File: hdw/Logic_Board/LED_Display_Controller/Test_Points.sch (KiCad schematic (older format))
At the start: 12 parts, among them J3001 USB UART, J3002 WIFI UART, J3003 FLASH SPI, J3004 Panel TP

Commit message: Finished first pass of digikey part numbers
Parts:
- added TP3009, TP3010: TP, symbol Custom_Library:TP
- J3004: Digi-Key PN (none) -> S2011EC-17-ND
- TP3007: value TestPoint -> TP
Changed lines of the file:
@@
 AR Path="/5BBF5233/5BBFA781" Ref="TP3007"  Part="1"
 F 0 "TP3007" H 4680 6260 50  0000 C CNN
-F 1 "TestPoint" H 4680 6250 50  0001 C CNN
+F 1 "TP" H 4680 6250 50  0001 C CNN
 F 2 "" H 4880 6050 50  0001 C CNN
 F 3 "~" H 4880 6050 50  0001 C CNN
@@
 F 2 "" H 8670 3350 50  0001 C CNN
 F 3 "~" H 8670 3350 50  0001 C CNN
+F 4 "S2011EC-17-ND" H 0   0   50  0001 C CNN "Digi-Key PN"
 	1    8670 3350
 	1    0    0    -1
@@
 	1    0    0    -1
 $EndComp
+$Comp
+L Custom_Library:TP TP?
+U 1 1 5C0ACA52
+P 1260 5980
+AR Path="/5BAAE0FA/5C0ACA52" Ref="TP?"  Part="1"
+AR Path="/5BBF5233/5C0ACA52" Ref="TP3010"  Part="1"
+F 0 "TP3010" H 1260 6130 50  0000 C CNN
+F 1 "TP" H 1260 6130 50  0001 C CNN
+F 2 "" H 1260 5980 60  0000 C CNN
+F 3 "" H 1260 5980 60  0000 C CNN
+	1    1260 5980
+	1    0    0    -1
+$EndComp
+$Comp
+L power:GND #PWR?
+U 1 1 5C0ACA59
+P 1260 5980
+AR Path="/5BAAE0FA/5C0ACA59" Ref="#PWR?"  Part="1"
+AR Path="/5BBF5233/5C0ACA59" Ref="#PWR03015"  Part="1"
+F 0 "#PWR03015" H 1260 5730 50  0001 C CNN
+F 1 "GND" H 1260 5830 50  0000 C CNN
+F 2 "" H 1260 5980 50  0001 C CNN
+F 3 "" H 1260 5980 50  0001 C CNN
+	1    1260 5980
+	1    0    0    -1
+$EndComp
+$Comp
+L Custom_Library:TP TP?
+U 1 1 5C0ACABF
+P 900 5980
+AR Path="/5BAAE0FA/5C0ACABF" Ref="TP?"  Part="1"
+AR Path="/5BBF5233/5C0ACABF" Ref="TP3009"  Part="1"
+F 0 "TP3009" H 900 6130 50  0000 C CNN
+F 1 "TP" H 900 6130 50  0001 C CNN
+F 2 "" H 900 5980 60  0000 C CNN
+F 3 "" H 900 5980 60  0000 C CNN
+	1    900  5980
+	1    0    0    -1
+$EndComp
+$Comp
+L power:GND #PWR?
+U 1 1 5C0ACAC6
+P 900 5980
+AR Path="/5BAAE0FA/5C0ACAC6" Ref="#PWR?"  Part="1"
+AR Path="/5BBF5233/5C0ACAC6" Ref="#PWR03014"  Part="1"
+F 0 "#PWR03014" H 900 5730 50  0001 C CNN
+F 1 "GND" H 900 5830 50  0000 C CNN
+F 2 "" H 900 5980 50  0001 C CNN
+F 3 "" H 900 5980 50  0001 C CNN
+	1    900  5980
+	1    0    0    -1
+$EndComp

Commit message: First pass assignment of footprints to all components
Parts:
- J3001, J3002: footprint (none) -> Pin_Headers:Pin_Header_Straight_1x03_Pitch2.54mm
- J3003: footprint (none) -> Pin_Headers:Pin_Header_Straight_1x04_Pitch2.54mm
- J3004: footprint (none) -> Pin_Headers:Pin_Header_Straight_2x17_Pitch2.54mm
- TP3001, TP3007, TP3009, TP3010: footprint (none) -> Pin_Headers:Pin_Header_Angled_1x01_Pitch2.54mm
- TP3002, TP3003, TP3004, TP3005, TP3006, TP3008: footprint (none) -> Measurement_Points:Measurement_Point_Round-SMD-Pad_Small
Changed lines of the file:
@@
 F 0 "J3001" H 2060 2042 50  0000 L CNN
 F 1 "USB UART" H 2060 1951 50  0000 L CNN
-F 2 "" H 1980 2000 50  0001 C CNN
+F 2 "Pin_Headers:Pin_Header_Straight_1x03_Pitch2.54mm" H 1980 2000 50  0001 C CNN
 F 3 "~" H 1980 2000 50  0001 C CNN
 	1    1980 2000
@@
 F 0 "TP3001" H 1640 6130 50  0000 C CNN
 F 1 "TP" H 1640 6130 50  0001 C CNN
-F 2 "" H 1640 5980 60  0000 C CNN
+F 2 "Pin_Headers:Pin_Header_Angled_1x01_Pitch2.54mm" H 1640 5980 60  0001 C CNN
 F 3 "" H 1640 5980 60  0000 C CNN
 	1    1640 5980
@@
 F 0 "TP3002" H 2040 6130 50  0000 C CNN
 F 1 "TP" H 2040 6130 50  0001 C CNN
-F 2 "" H 2040 5980 60  0000 C CNN
+F 2 "Measurement_Points:Measurement_Point_Round-SMD-Pad_Small" H 2040 5980 60  0001 C CNN
 F 3 "" H 2040 5980 60  0000 C CNN
 	1    2040 5980
@@
 F 0 "TP3003" H 2480 6130 50  0000 C CNN
 F 1 "TP" H 2480 6130 50  0001 C CNN
-F 2 "" H 2480 5980 60  0000 C CNN
+F 2 "Measurement_Points:Measurement_Point_Round-SMD-Pad_Small" H 2480 5980 60  0001 C CNN
 F 3 "" H 2480 5980 60  0000 C CNN
 	1    2480 5980
@@
 F 0 "TP3007" H 4680 6260 50  0000 C CNN
 F 1 "TP" H 4680 6250 50  0001 C CNN
-F 2 "" H 4880 6050 50  0001 C CNN
+F 2 "Pin_Headers:Pin_Header_Angled_1x01_Pitch2.54mm" H 4880 6050 50  0001 C CNN
 F 3 "~" H 4880 6050 50  0001 C CNN
 	1    4680 6050
@@
 F 0 "TP3008" H 5330 6160 50  0000 C CNN
 F 1 "TP" H 5330 6160 50  0001 C CNN
-F 2 "" H 5330 6010 60  0000 C CNN
+F 2 "Measurement_Points:Measurement_Point_Round-SMD-Pad_Small" H 5330 6010 60  0001 C CNN
 F 3 "" H 5330 6010 60  0000 C CNN
 	1    5330 6010
@@
 F 0 "J3004" H 8720 4250 50  0000 C CNN
 F 1 "Panel TP" H 8720 2450 50  0000 C CNN
-F 2 "" H 8670 3350 50  0001 C CNN
+F 2 "Pin_Headers:Pin_Header_Straight_2x17_Pitch2.54mm" H 8670 3350 50  0001 C CNN
 F 3 "~" H 8670 3350 50  0001 C CNN
 F 4 "S2011EC-17-ND" H 0   0   50  0001 C CNN "Digi-Key PN"
@@
 F 0 "TP3004" H 2940 6130 50  0000 C CNN
 F 1 "TP" H 2940 6130 50  0001 C CNN
-F 2 "" H 2940 5980 60  0000 C CNN
+F 2 "Measurement_Points:Measurement_Point_Round-SMD-Pad_Small" H 2940 5980 60  0001 C CNN
 F 3 "" H 2940 5980 60  0000 C CNN
 	1    2940 5980
@@
 F 0 "J3002" H 3700 2042 50  0000 L CNN
 F 1 "WIFI UART" H 3700 1951 50  0000 L CNN
-F 2 "" H 3620 2000 50  0001 C CNN
+F 2 "Pin_Headers:Pin_Header_Straight_1x03_Pitch2.54mm" H 3620 2000 50  0001 C CNN
 F 3 "~" H 3620 2000 50  0001 C CNN
 	1    3620 2000
@@
 F 0 "J3003" H 5260 1992 50  0000 L CNN
 F 1 "FLASH SPI" H 5260 1901 50  0000 L CNN
-F 2 "" H 5180 2000 50  0001 C CNN
+F 2 "Pin_Headers:Pin_Header_Straight_1x04_Pitch2.54mm" H 5180 2000 50  0001 C CNN
 F 3 "~" H 5180 2000 50  0001 C CNN
 	1    5180 2000
@@
 F 0 "TP3005" H 3340 6130 50  0000 C CNN
 F 1 "TP" H 3340 6130 50  0001 C CNN
-F 2 "" H 3340 5980 60  0000 C CNN
+F 2 "Measurement_Points:Measurement_Point_Round-SMD-Pad_Small" H 3340 5980 60  0001 C CNN
 F 3 "" H 3340 5980 60  0000 C CNN
 	1    3340 5980
@@
 F 0 "TP3006" H 3680 6130 50  0000 C CNN
 F 1 "TP" H 3680 6130 50  0001 C CNN
-F 2 "" H 3680 5980 60  0000 C CNN
+F 2 "Measurement_Points:Measurement_Point_Round-SMD-Pad_Small" H 3680 5980 60  0001 C CNN
 F 3 "" H 3680 5980 60  0000 C CNN
 	1    3680 5980
@@
 F 0 "TP3010" H 1260 6130 50  0000 C CNN
 F 1 "TP" H 1260 6130 50  0001 C CNN
-F 2 "" H 1260 5980 60  0000 C CNN
+F 2 "Pin_Headers:Pin_Header_Angled_1x01_Pitch2.54mm" H 1260 5980 60  0001 C CNN
 F 3 "" H 1260 5980 60  0000 C CNN
 	1    1260 5980
@@
 F 0 "TP3009" H 900 6130 50  0000 C CNN
 F 1 "TP" H 900 6130 50  0001 C CNN
-F 2 "" H 900 5980 60  0000 C CNN
+F 2 "Pin_Headers:Pin_Header_Angled_1x01_Pitch2.54mm" H 900 5980 60  0001 C CNN
 F 3 "" H 900 5980 60  0000 C CNN
 	1    900  5980

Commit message: Resolved a few library dependencies
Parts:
- TP3001, TP3002, TP3003, TP3004, TP3005, TP3006, TP3008, TP3009, TP3010: symbol Custom_Library:TP -> LED_Display_Local_Library:TP
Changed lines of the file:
@@
 $EndComp
 $Comp
-L Custom_Library:TP TP?
+L LED_Display_Local_Library:TP TP?
 U 1 1 5BBF8ECA
 P 1640 5980
@@
 $EndComp
 $Comp
-L Custom_Library:TP TP?
+L LED_Display_Local_Library:TP TP?
 U 1 1 5BBF9883
 P 2040 5980
@@
 $EndComp
 $Comp
-L Custom_Library:TP TP?
+L LED_Display_Local_Library:TP TP?
 U 1 1 5BBF98E5
 P 2480 5980
@@
 $EndComp
 $Comp
-L Custom_Library:TP TP3008
+L LED_Display_Local_Library:TP TP3008
 U 1 1 5BBFB09C
 P 5330 6010
@@
 $EndComp
 $Comp
-L Custom_Library:+5V_USB #PWR03011
+L LED_Display_Local_Library:+5V_USB #PWR03011
 U 1 1 5BBFB102
 P 5330 6010
@@
 	9050 4150 8970 4150
 $Comp
-L Custom_Library:TP TP?
+L LED_Display_Local_Library:TP TP?
 U 1 1 5BD1E3B2
 P 2940 5980
@@
 FLASH_MISO
 $Comp
-L Custom_Library:TP TP?
+L LED_Display_Local_Library:TP TP?
 U 1 1 5BF9B560
 P 3340 5980
@@
 $EndComp
 $Comp
-L Custom_Library:TP TP?
+L LED_Display_Local_Library:TP TP?
 U 1 1 5BF9B60D
 P 3680 5980
@@
 $EndComp
 $Comp
-L Custom_Library:+5.5V #PWR03008
+L LED_Display_Local_Library:+5.5V #PWR03008
 U 1 1 5BF9B68F
 P 3680 5980
@@
 $EndComp
 $Comp
-L Custom_Library:TP TP?
+L LED_Display_Local_Library:TP TP?
 U 1 1 5C0ACA52
 P 1260 5980
@@
 $EndComp
 $Comp
-L Custom_Library:TP TP?
+L LED_Display_Local_Library:TP TP?
 U 1 1 5C0ACABF
 P 900 5980

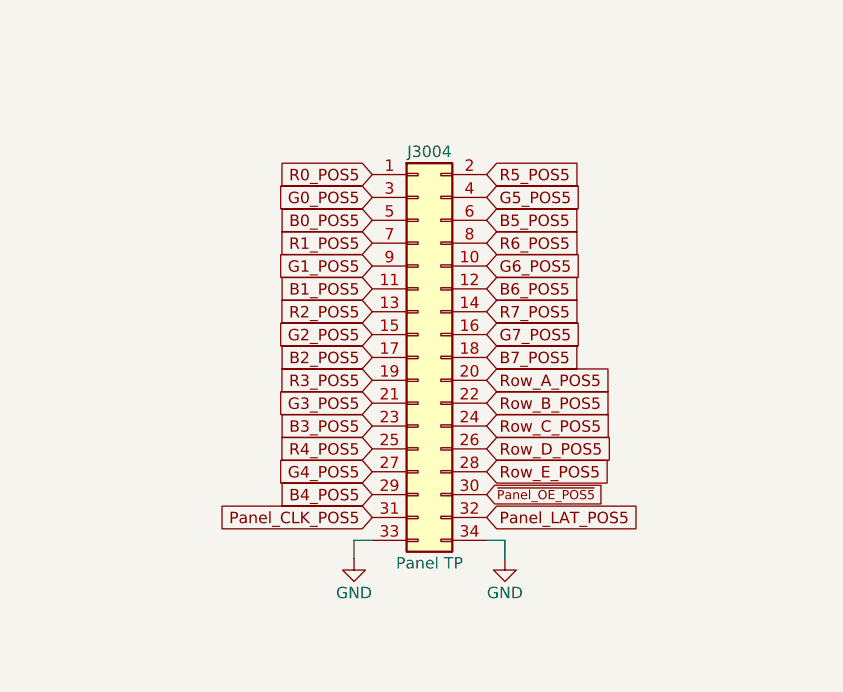
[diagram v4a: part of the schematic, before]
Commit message: Placed more parts, added some labels
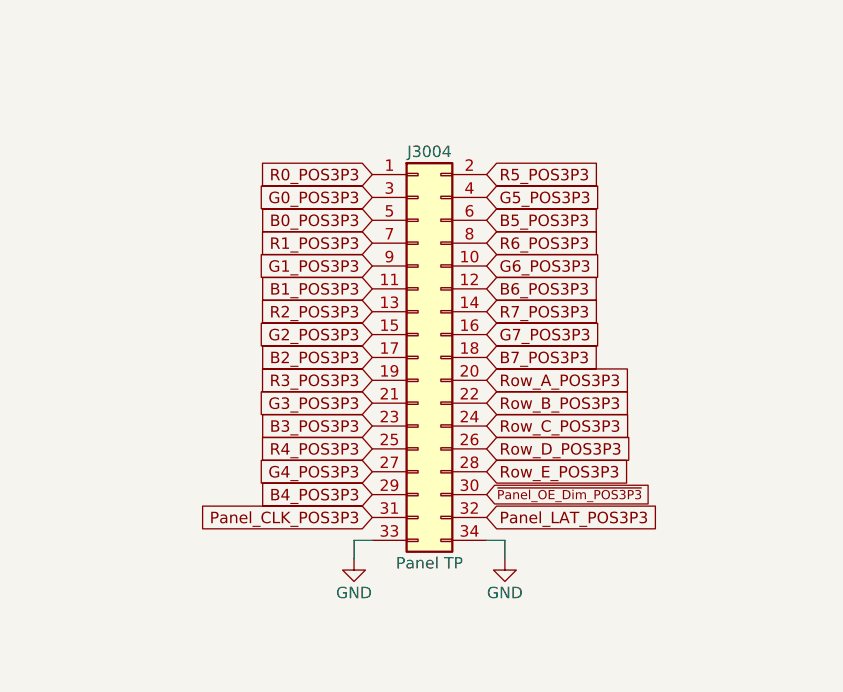
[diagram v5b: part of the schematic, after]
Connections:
- net B0_POS5 renamed B0_POS3P3
- net B1_POS5 renamed B1_POS3P3
- net B2_POS5 renamed B2_POS3P3
- net B3_POS5 renamed B3_POS3P3
- net B4_POS5 renamed B4_POS3P3
- net B5_POS5 renamed B5_POS3P3
- net B6_POS5 renamed B6_POS3P3
- net B7_POS5 renamed B7_POS3P3
- net G0_POS5 renamed G0_POS3P3
- net G1_POS5 renamed G1_POS3P3
- net G2_POS5 renamed G2_POS3P3
- net G3_POS5 renamed G3_POS3P3
- net G4_POS5 renamed G4_POS3P3
- net G5_POS5 renamed G5_POS3P3
- net G6_POS5 renamed G6_POS3P3
- net G7_POS5 renamed G7_POS3P3
- net Panel_CLK_POS5 renamed Panel_CLK_POS3P3
- net Panel_LAT_POS5 renamed Panel_LAT_POS3P3
- net R0_POS5 renamed R0_POS3P3
- net R1_POS5 renamed R1_POS3P3
- net R2_POS5 renamed R2_POS3P3
- net R3_POS5 renamed R3_POS3P3
- net R4_POS5 renamed R4_POS3P3
- net R5_POS5 renamed R5_POS3P3
- net R6_POS5 renamed R6_POS3P3
- net R7_POS5 renamed R7_POS3P3
- net Row_A_POS5 renamed Row_A_POS3P3
- net Row_B_POS5 renamed Row_B_POS3P3
- net Row_C_POS5 renamed Row_C_POS3P3
- net Row_D_POS5 renamed Row_D_POS3P3
- net Row_E_POS5 renamed Row_E_POS3P3
- net ~Panel_OE_POS5 renamed ~Panel_OE_Dim_POS3P3
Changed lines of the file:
@@
 $EndComp
 Text GLabel 8970 3250 2    50   Input ~ 0
-G7_POS5
+G7_POS3P3
 Text GLabel 8970 3350 2    50   Input ~ 0
-B7_POS5
+B7_POS3P3
 Text GLabel 8970 3150 2    50   Input ~ 0
-R7_POS5
+R7_POS3P3
 Text GLabel 8970 2950 2    50   Input ~ 0
-G6_POS5
+G6_POS3P3
 Text GLabel 8970 3050 2    50   Input ~ 0
-B6_POS5
+B6_POS3P3
 Text GLabel 8970 2850 2    50   Input ~ 0
-R6_POS5
+R6_POS3P3
 Text GLabel 8970 2650 2    50   Input ~ 0
-G5_POS5
+G5_POS3P3
 Text GLabel 8970 2750 2    50   Input ~ 0
-B5_POS5
+B5_POS3P3
 Text GLabel 8970 2550 2    50   Input ~ 0
-R5_POS5
+R5_POS3P3
 Text GLabel 8470 3850 0    50   Input ~ 0
-G4_POS5
+G4_POS3P3
 Text GLabel 8470 3950 0    50   Input ~ 0
-B4_POS5
+B4_POS3P3
 Text GLabel 8470 3750 0    50   Input ~ 0
-R4_POS5
+R4_POS3P3
 Text GLabel 8470 3550 0    50   Input ~ 0
-G3_POS5
+G3_POS3P3
 Text GLabel 8470 3650 0    50   Input ~ 0
-B3_POS5
+B3_POS3P3
 Text GLabel 8470 3450 0    50   Input ~ 0
-R3_POS5
+R3_POS3P3
 Text GLabel 8470 3250 0    50   Input ~ 0
-G2_POS5
+G2_POS3P3
 Text GLabel 8470 3350 0    50   Input ~ 0
-B2_POS5
+B2_POS3P3
 Text GLabel 8470 3150 0    50   Input ~ 0
-R2_POS5
+R2_POS3P3
 Text GLabel 8470 2950 0    50   Input ~ 0
-G1_POS5
+G1_POS3P3
 Text GLabel 8470 2650 0    50   Input ~ 0
-G0_POS5
+G0_POS3P3
 Text GLabel 8470 3050 0    50   Input ~ 0
-B1_POS5
+B1_POS3P3
 Text GLabel 8470 2850 0    50   Input ~ 0
-R1_POS5
+R1_POS3P3
 Text GLabel 8470 2750 0    50   Input ~ 0
-B0_POS5
+B0_POS3P3
 Text GLabel 8470 2550 0    50   Input ~ 0
-R0_POS5
+R0_POS3P3
 Text GLabel 8970 4050 2    50   Input ~ 0
-Panel_LAT_POS5
+Panel_LAT_POS3P3
+Text GLabel 8470 4050 0    50   Input ~ 0
+Panel_CLK_POS3P3
+Text GLabel 8970 3650 2    50   Input ~ 0
+Row_C_POS3P3
+Text GLabel 8970 3850 2    50   Input ~ 0
+Row_E_POS3P3
+Text GLabel 8970 3750 2    50   Input ~ 0
+Row_D_POS3P3
+Text GLabel 8970 3550 2    50   Input ~ 0
+Row_B_POS3P3
+Text GLabel 8970 3450 2    50   Input ~ 0
+Row_A_POS3P3
 Text GLabel 8970 3950 2    40   Input ~ 0
-~Panel_OE_POS5
-Text GLabel 8470 4050 0    50   Input ~ 0
-Panel_CLK_POS5
-Text GLabel 8970 3650 2    50   Input ~ 0
-Row_C_POS5
-Text GLabel 8970 3850 2    50   Input ~ 0
-Row_E_POS5
-Text GLabel 8970 3750 2    50   Input ~ 0
-Row_D_POS5
-Text GLabel 8970 3550 2    50   Input ~ 0
-Row_B_POS5
-Text GLabel 8970 3450 2    50   Input ~ 0
-Row_A_POS5
+~Panel_OE_Dim_POS3P3
 $EndSCHEMATC

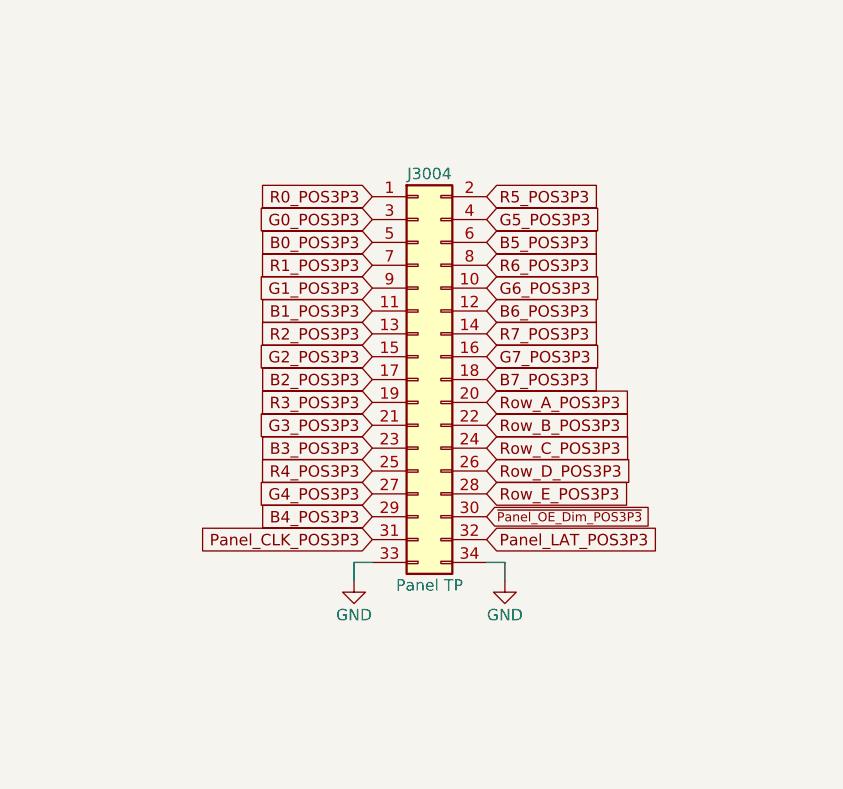
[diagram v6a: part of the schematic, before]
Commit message: Routed a bunch of traces
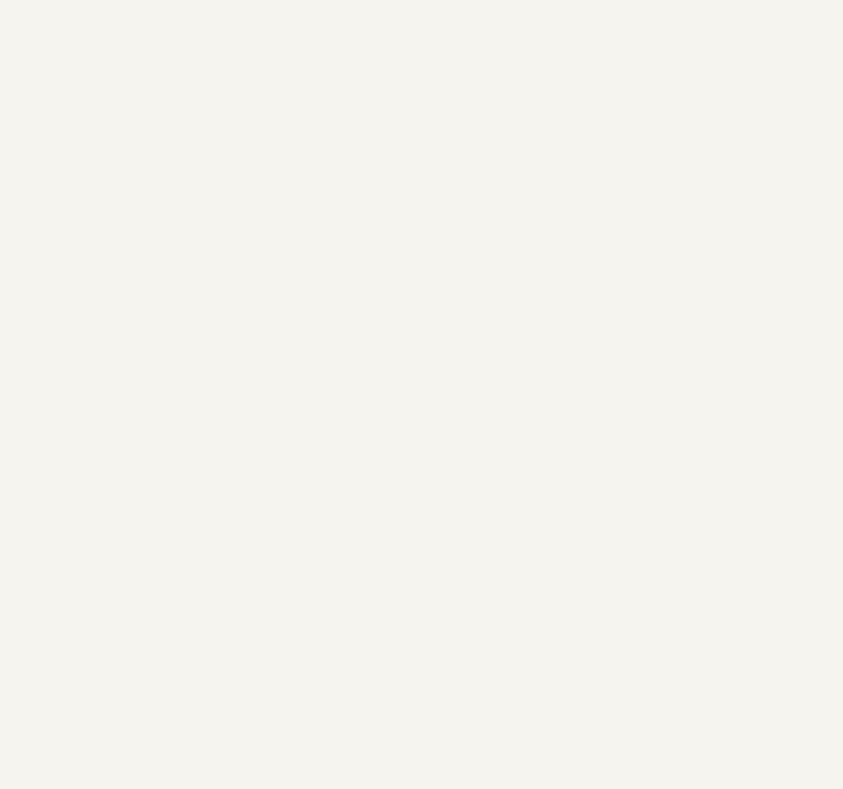
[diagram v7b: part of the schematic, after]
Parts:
- removed J3004: Panel TP, Pin_Headers:Pin_Header_Straight_2x17_Pitch2.54mm, symbol Connector_Generic:Conn_02x17_Odd_Even
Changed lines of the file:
@@
 	1    0    0    -1
 $EndComp
-Wire Wire Line
-	9050 4150 8970 4150
-Wire Wire Line
-	9050 4230 9050 4150
-$Comp
-L power:GND #PWR03013
-U 1 1 5BC07949
-P 9050 4230
-F 0 "#PWR03013" H 9050 3980 50  0001 C CNN
-F 1 "GND" H 9050 4080 50  0000 C CNN
-F 2 "" H 9050 4230 50  0001 C CNN
-F 3 "" H 9050 4230 50  0001 C CNN
-	1    9050 4230
-	1    0    0    -1
-$EndComp
-Wire Wire Line
-	8390 4150 8470 4150
-Wire Wire Line
-	8390 4230 8390 4150
-$Comp
-L power:GND #PWR03012
-U 1 1 5BC078FB
-P 8390 4230
-F 0 "#PWR03012" H 8390 3980 50  0001 C CNN
-F 1 "GND" H 8390 4080 50  0000 C CNN
-F 2 "" H 8390 4230 50  0001 C CNN
-F 3 "" H 8390 4230 50  0001 C CNN
-	1    8390 4230
-	1    0    0    -1
-$EndComp
-$Comp
-L Connector_Generic:Conn_02x17_Odd_Even J3004
-U 1 1 5BC06F5E
-P 8670 3350
-F 0 "J3004" H 8720 4250 50  0000 C CNN
-F 1 "Panel TP" H 8720 2450 50  0000 C CNN
-F 2 "Pin_Headers:Pin_Header_Straight_2x17_Pitch2.54mm" H 8670 3350 50  0001 C CNN
-F 3 "~" H 8670 3350 50  0001 C CNN
-F 4 "S2011EC-17-ND" H 0   0   50  0001 C CNN "Digi-Key PN"
-	1    8670 3350
-	1    0    0    -1
-$EndComp
-Text GLabel 8970 3250 2    50   Input ~ 0
-G7_POS3P3
-Text GLabel 8970 3350 2    50   Input ~ 0
-B7_POS3P3
-Text GLabel 8970 3150 2    50   Input ~ 0
-R7_POS3P3
-Text GLabel 8970 2950 2    50   Input ~ 0
-G6_POS3P3
-Text GLabel 8970 3050 2    50   Input ~ 0
-B6_POS3P3
-Text GLabel 8970 2850 2    50   Input ~ 0
-R6_POS3P3
-Text GLabel 8970 2650 2    50   Input ~ 0
-G5_POS3P3
-Text GLabel 8970 2750 2    50   Input ~ 0
-B5_POS3P3
-Text GLabel 8970 2550 2    50   Input ~ 0
-R5_POS3P3
-Text GLabel 8470 3850 0    50   Input ~ 0
-G4_POS3P3
-Text GLabel 8470 3950 0    50   Input ~ 0
-B4_POS3P3
-Text GLabel 8470 3750 0    50   Input ~ 0
-R4_POS3P3
-Text GLabel 8470 3550 0    50   Input ~ 0
-G3_POS3P3
-Text GLabel 8470 3650 0    50   Input ~ 0
-B3_POS3P3
-Text GLabel 8470 3450 0    50   Input ~ 0
-R3_POS3P3
-Text GLabel 8470 3250 0    50   Input ~ 0
-G2_POS3P3
-Text GLabel 8470 3350 0    50   Input ~ 0
-B2_POS3P3
-Text GLabel 8470 3150 0    50   Input ~ 0
-R2_POS3P3
-Text GLabel 8470 2950 0    50   Input ~ 0
-G1_POS3P3
-Text GLabel 8470 2650 0    50   Input ~ 0
-G0_POS3P3
-Text GLabel 8470 3050 0    50   Input ~ 0
-B1_POS3P3
-Text GLabel 8470 2850 0    50   Input ~ 0
-R1_POS3P3
-Text GLabel 8470 2750 0    50   Input ~ 0
-B0_POS3P3
-Text GLabel 8470 2550 0    50   Input ~ 0
-R0_POS3P3
-Text GLabel 8970 4050 2    50   Input ~ 0
-Panel_LAT_POS3P3
-Text GLabel 8470 4050 0    50   Input ~ 0
-Panel_CLK_POS3P3
-Text GLabel 8970 3650 2    50   Input ~ 0
-Row_C_POS3P3
-Text GLabel 8970 3850 2    50   Input ~ 0
-Row_E_POS3P3
-Text GLabel 8970 3750 2    50   Input ~ 0
-Row_D_POS3P3
-Text GLabel 8970 3550 2    50   Input ~ 0
-Row_B_POS3P3
-Text GLabel 8970 3450 2    50   Input ~ 0
-Row_A_POS3P3
-Text GLabel 8970 3950 2    40   Input ~ 0
-~Panel_OE_Dim_POS3P3
 $EndSCHEMATC
